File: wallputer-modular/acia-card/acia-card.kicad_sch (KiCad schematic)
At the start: 1 part

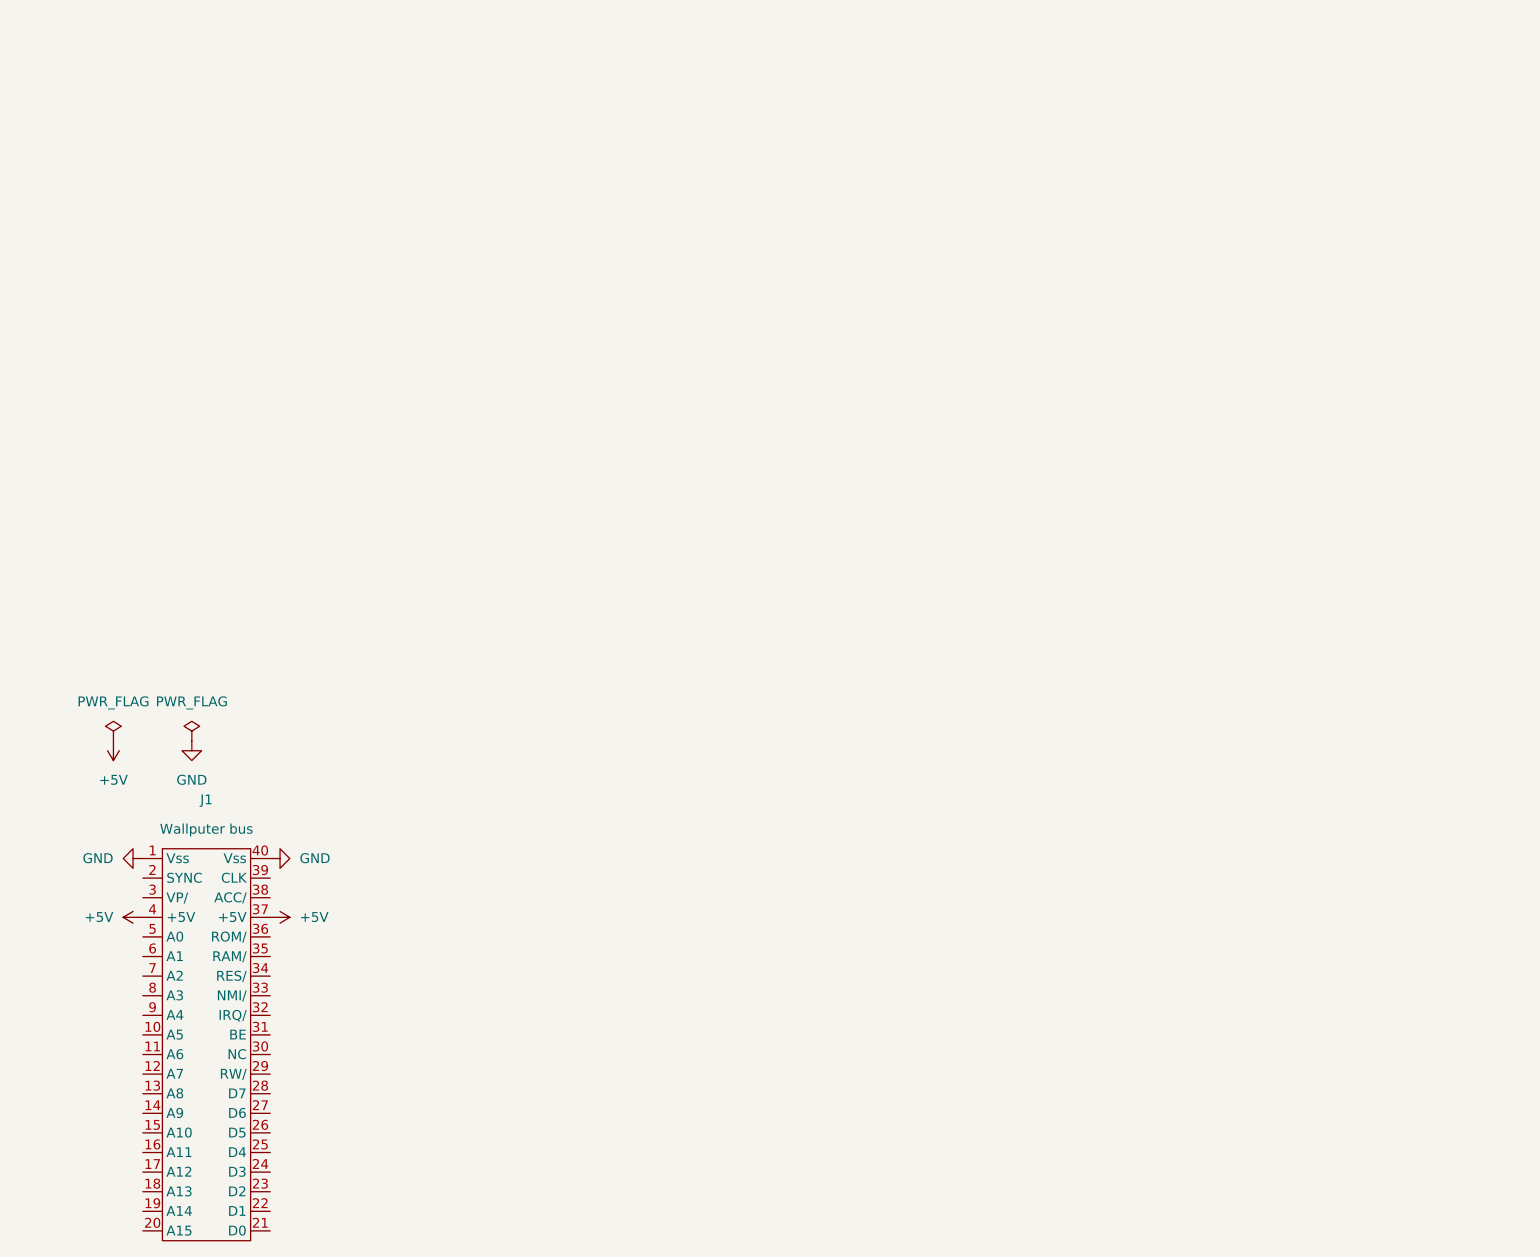
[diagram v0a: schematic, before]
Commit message: copy parts of single board
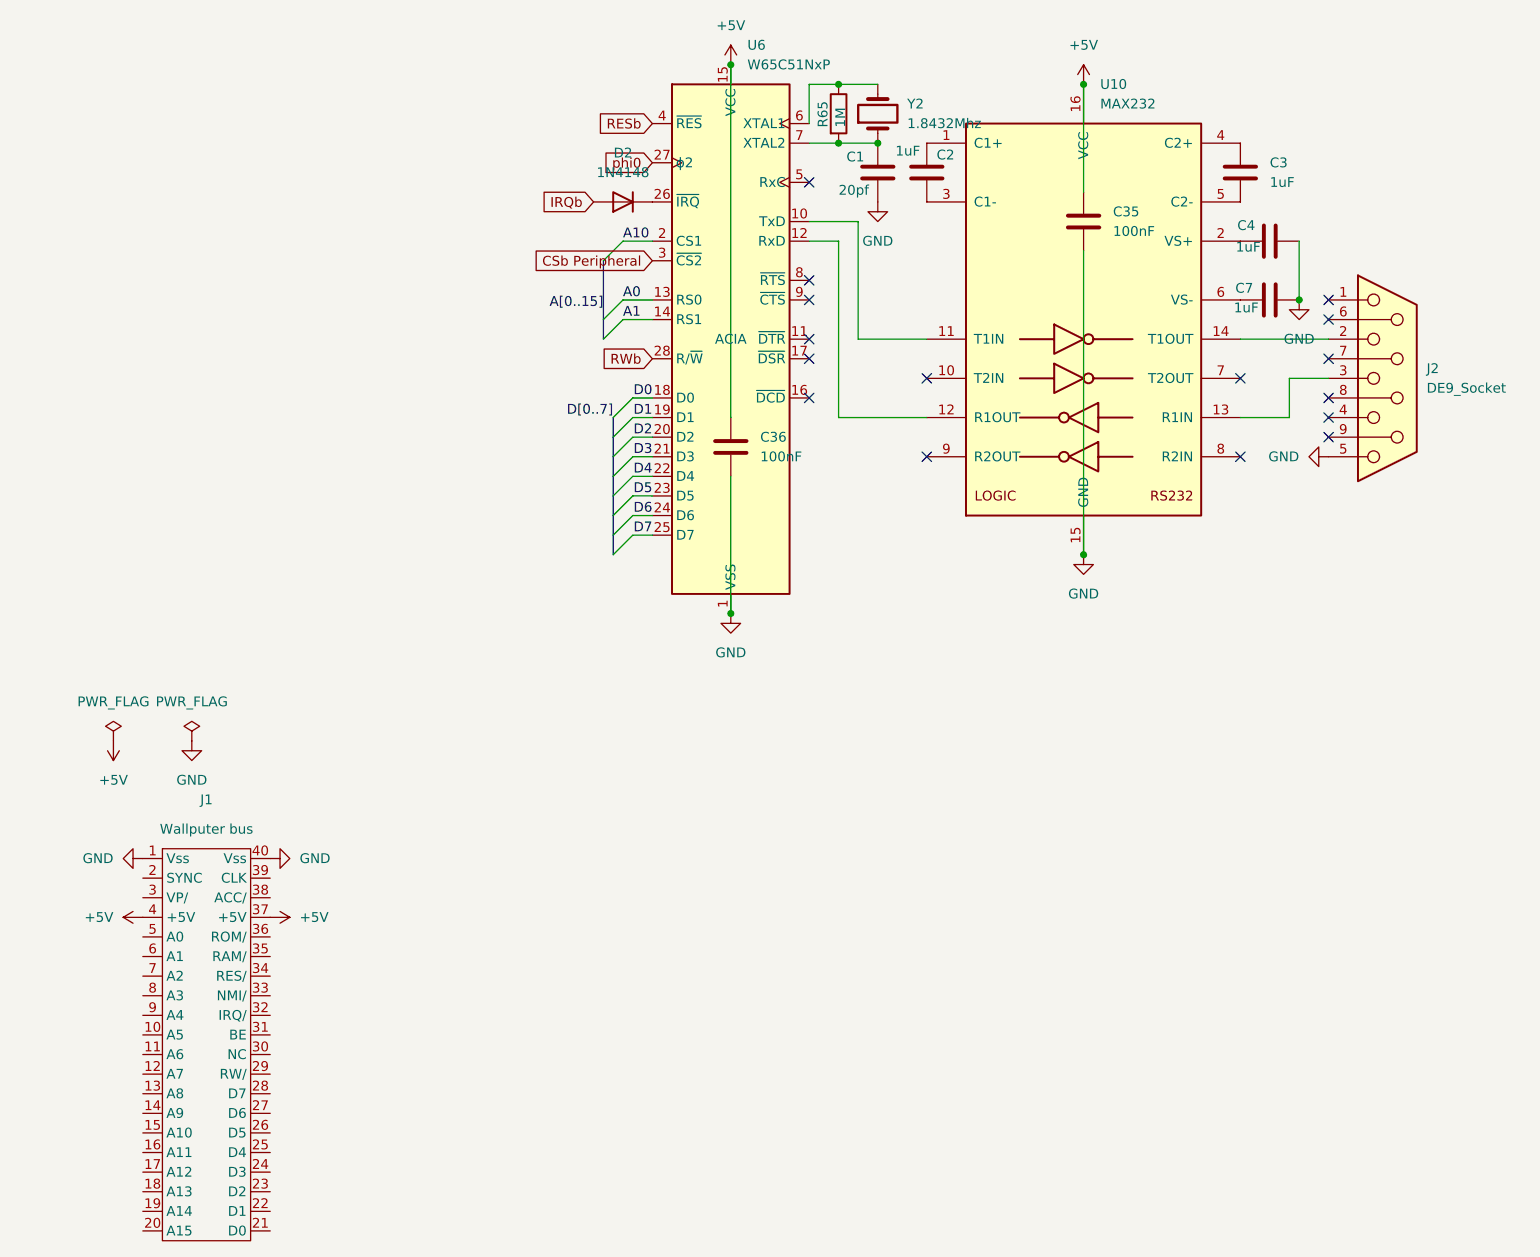
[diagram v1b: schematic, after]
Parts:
- added C1: 20pf, Capacitor_THT:C_Disc_D5.0mm_W2.5mm_P5.00mm, symbol Device:C
- added C2, C3, C4, C7: 1uF, Capacitor_THT:C_Disc_D5.0mm_W2.5mm_P5.00mm, symbol Device:C
- added C35, C36: 100nF, Capacitor_THT:C_Disc_D5.0mm_W2.5mm_P5.00mm, symbol Device:C
- added D2: 1N4148, Diode_THT:D_DO-35_SOD27_P7.62mm_Horizontal, symbol Diode:1N4148
- added J2: DE9_Socket, Connector_Dsub:DSUB-9_Pins_Horizontal_P2.77x2.84mm_EdgePinOffset4.94mm_Housed_MountingHolesOffset4.94mm, symbol Connector:DE9_Socket
- added R65: 1M, Resistor_THT:R_Axial_DIN0204_L3.6mm_D1.6mm_P2.54mm_Vertical, symbol Device:R
- added U10: MAX232, Package_DIP:DIP-16_W7.62mm_Socket, symbol Interface_UART:MAX232
- added U6: W65C51NxP, Package_DIP:DIP-28_W15.24mm, symbol 65xx-library:W65C51NxP
- added Y2: 1.8432Mhz, Crystal:Crystal_HC18-U_Vertical, symbol Device:Crystal
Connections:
- net +5V: now also C35.1, C36.1, U10.16 (VCC), U6.15 (VCC)
- net GND: now also C1.2, C35.2, C36.2, C4.2, C7.2, J2.5, U10.15 (GND), U6.1 (VSS)
- new net: C2.1, U10.1 (C1+)
- new net: U10.11 (T1IN), U6.10 (TxD)
- new net: U10.12 (R1OUT), U6.12 (RxD)
- new net: J2.3, U10.13 (R1IN)
- new net: J2.2, U10.14 (T1OUT)
- new net: C4.1, U10.2 (VS+)
- new net: C2.2, U10.3 (C1-)
- new net: C3.1, U10.4 (C2+)
- new net: C3.2, U10.5 (C2-)
- new net: C7.1, U10.6 (VS-)
- new net: D2.1 (K), U6.26 (~{IRQ})
- new net: R65.1, U6.6 (XTAL1), Y2.2
- new net: C1.1, R65.2, U6.7 (XTAL2), Y2.1
- new net A0: U6.13 (RS0)
- new net A1: U6.14 (RS1)
- new net A10: U6.2 (CS1)
- new net CSb Peripheral: U6.3 (~{CS2})
- new net D0: U6.18 (D0)
- new net D1: U6.19 (D1)
- new net D2: U6.20 (D2)
- new net D3: U6.21 (D3)
- new net D4: U6.22 (D4)
- new net D5: U6.23 (D5)
- new net D6: U6.24 (D6)
- new net D7: U6.25 (D7)
- new net IRQb: D2.2 (A)
- new net RESb: U6.4 (~{RES})
- new net RWb: U6.28 (R/~{W})
- new net phi0: U6.27 (ϕ2)
- no-connect marks 0 -> 16

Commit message: implement acia card
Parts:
- added D1: Red, LED_THT:LED_D1.8mm_W3.3mm_H2.4mm, symbol Device:LED
- added D3: Green, LED_THT:LED_D1.8mm_W3.3mm_H2.4mm, symbol Device:LED
- added Q1, Q2: BSS84, Package_TO_SOT_SMD:SOT-23, symbol Transistor_FET:BSS84
- added R1, R3: 100k, Resistor_THT:R_Axial_DIN0204_L3.6mm_D1.6mm_P2.54mm_Vertical, symbol Device:R
- added R2, R4: 220, Resistor_THT:R_Axial_DIN0204_L3.6mm_D1.6mm_P2.54mm_Vertical, symbol Device:R
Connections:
- net CSb Peripheral is gone; now on net ACC/: U6.3 (~{CS2})
- net IRQb is gone; now on net IRQ/: D2.2 (A)
- net RESb is gone; now on net RES/: U6.4 (~{RES})
- net RWb is gone; now on net RW/: U6.28 (R/~{W})
- net phi0 is gone; now on net CLK: U6.27 (ϕ2)
- net +5V: now also J2.9, Q1.2 (S), Q2.2 (S), R1.2, R3.2
- net A0: now also J1.5 (A0)
- net A1: now also J1.6 (A1)
- net A10: now also J1.15 (A10)
- net D0: now also J1.21 (D0)
- net D1: now also J1.22 (D1)
- net D2: now also J1.23 (D2)
- net D3: now also J1.24 (D3)
- net D4: now also J1.25 (D4)
- net D5: now also J1.26 (D5)
- net D6: now also J1.27 (D6)
- net D7: now also J1.28 (D7)
- net GND: now also D1.1 (K), D3.1 (K)
- net at U10.11 (T1IN), U6.10 (TxD): now also Q1.1 (G), R1.1
- net at U10.12 (R1OUT), U6.12 (RxD): now also Q2.1 (G), R3.1
- net A5: now reaches J1.10 (A5)
- net A6: now reaches J1.11 (A6)
- net A7: now reaches J1.12 (A7)
- net A8: now reaches J1.13 (A8)
- net A9: now reaches J1.14 (A9)
- net A11: now reaches J1.16 (A11)
- net A12: now reaches J1.17 (A12)
- net A13: now reaches J1.18 (A13)
- net A14: now reaches J1.19 (A14)
- net A15: now reaches J1.20 (A15)
- net RW/: now reaches J1.29 (RW/)
- net IRQ/: now reaches J1.32 (IRQ/)
- net RES/: now reaches J1.34 (RES/)
- net ACC/: now reaches J1.38 (ACC/)
- net CLK: now reaches J1.39 (CLK)
- net A2: now reaches J1.7 (A2)
- net A3: now reaches J1.8 (A3)
- net A4: now reaches J1.9 (A4)
- new net: D1.2 (A), R2.2
- new net: Q1.3 (D), R2.1
- new net: Q2.3 (D), R4.1
- new net: D3.2 (A), R4.2
- no-connect marks 16 -> 22
